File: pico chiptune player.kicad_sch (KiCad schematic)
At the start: 40 parts, among them J2 MicroSD, J3 Speaker_L, J4 Speaker_R, SW1 Play / Pause, SW2 Next, SW3 Previous, U1 AY-3-8910, U2 0.96"OLED_I2C, U3 PAM8403, U4 YM2149F

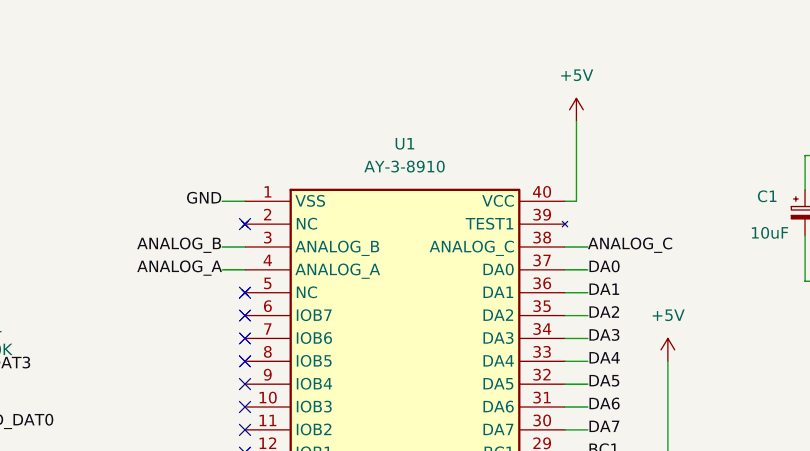
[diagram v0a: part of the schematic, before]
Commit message: sch, pcb, docs: fit YM2149F in both PSG sockets
U1 was specified as an AY-3-8910 while U4 was a YM2149F. Both share
CLOCK and the JP1 /SEL net, so bridging JP1 halved the clock on the
YM2149F only and put the two stereo channels an octave apart. Specify
both sockets as YM2149F so JP1 divides both chips together; document a
matched AY-3-8910 pair as an alternative with JP1 open.

Also relink PCB footprints U4, C9, C11, C12 and R9-R12 to their own
schematic symbols. They were copied from U1/C1/C2/R4 and still carried
those symbols' paths, which would cross-match parts on the next
"Update PCB from Schematic". Connectivity is unchanged.

Co-Authored-By: Claude Opus 5.5 <noreply@anthropic.com>
Claude-Session: https://claude.ai/code/session_01RJQvxUpHsHwrbMu8k2obTf
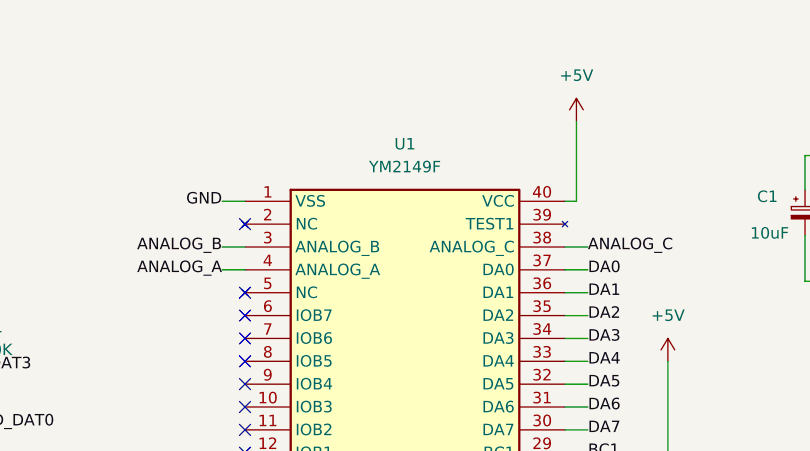
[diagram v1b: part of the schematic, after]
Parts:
- U1: value AY-3-8910 -> YM2149F
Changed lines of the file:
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@@
 		(company "MotionFxDesign")
 		(comment 1 "Terence Ang / MotionFxDesign")
-		(comment 2 "Hardware AY-3-8910 / YM2149 Chiptune Player")
+		(comment 2 "Hardware Dual YM2149F Chiptune Player")
 	)
 	(junction
@@
 			)
 		)
-		(property "Value" "AY-3-8910"
+		(property "Value" "YM2149F"
 			(at 167.64 33.02 0)
 			(show_name no)
@@
 			)
 		)
-		(property "Description" "AY-3-8910 3-voice Programmable Sound Generator (PSG), 40-pin DIP"
+		(property "Description" "YM2149F 3-voice Programmable Sound Generator (PSG), 40-pin DIP"
 			(at 167.64 60.96 0)
 			(hide yes)
